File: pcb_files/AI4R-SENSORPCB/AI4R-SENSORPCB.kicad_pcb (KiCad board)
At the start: 2 copper layers, 50 x 80 mm, 25 parts, among them J10 Conn_02x10_Odd_Even, J11 USB_B_Mini, J2 Conn_01x04, J3 Conn_01x04, J4 Conn_01x04, J5 Conn_01x04, J6 Conn_02x11_Odd_Even, J7 Conn_01x03, J8 Conn_01x10, J9 Conn_01x03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

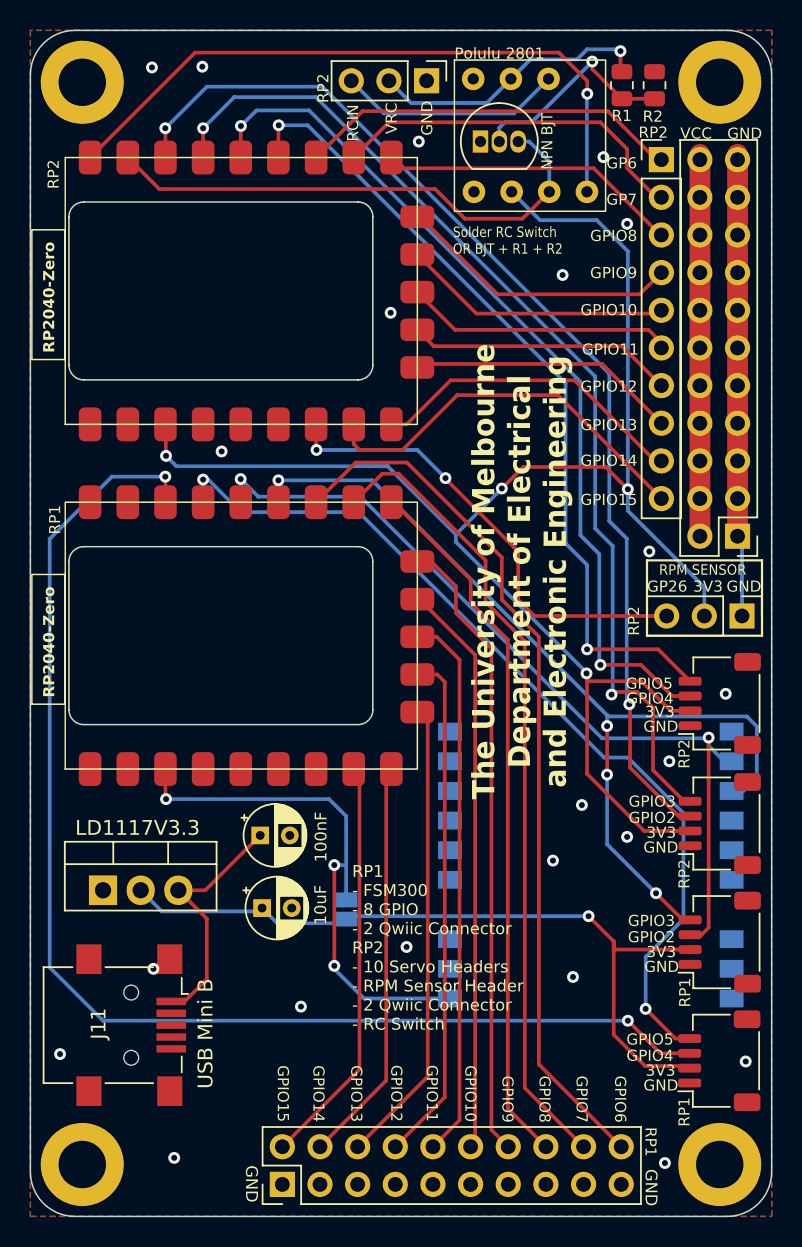
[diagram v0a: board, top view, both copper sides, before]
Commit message: fix gerber errors
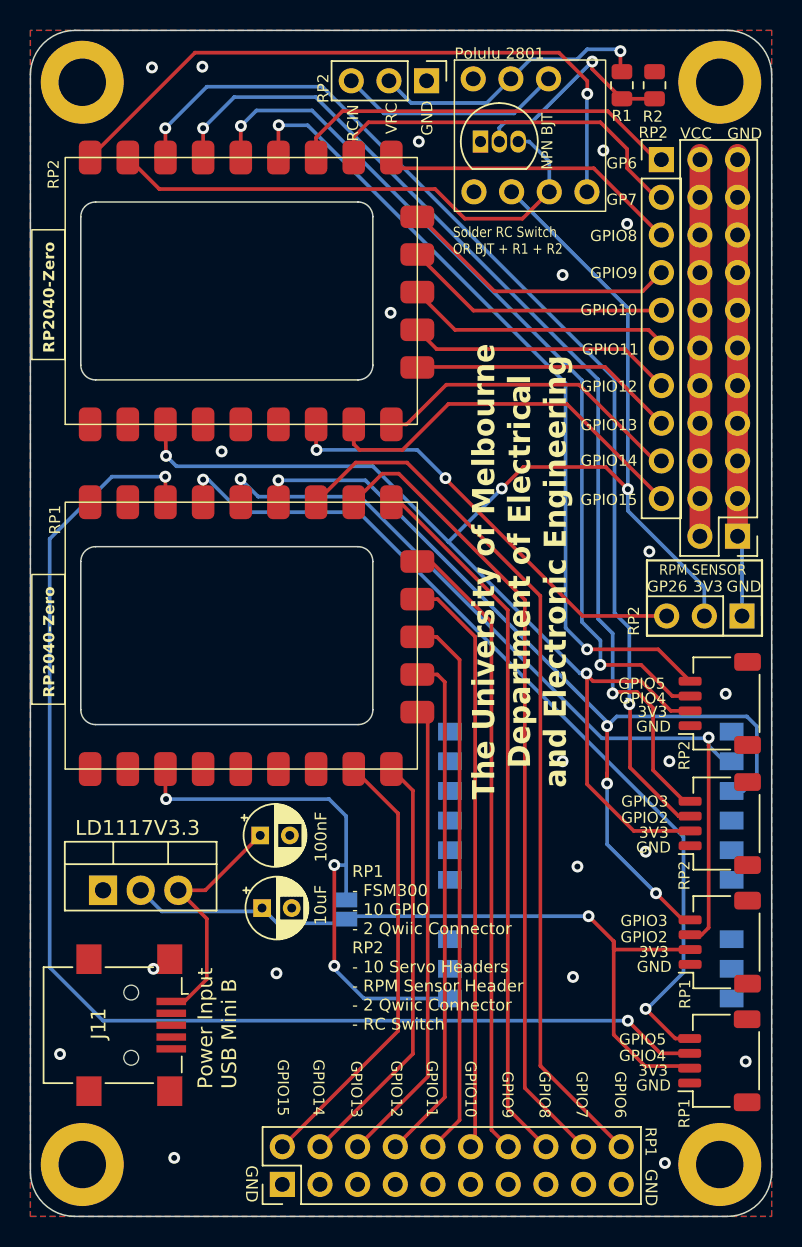
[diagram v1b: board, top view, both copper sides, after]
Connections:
- Q1 pad 3: GPIO1B -> GPIO2B
- RP2 pad 2: GPIO1B -> GPIO2B
- U2 pad 6: GPIO1B -> GPIO2B
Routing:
- net GPIO1B: track 80.3 -> 44.7 mm
- net GPIO2B: track 0.00 -> 35.6 mm
- net GP15: track 27.8 -> 29.9 mm
- net GP26B: track 31.9 -> 30.0 mm
- net 3V3B: track 111.0 -> 109.3 mm
- net GP14: track 27.5 -> 28.7 mm
- net GP10B: track 18.7 -> 17.8 mm
- net SCL2: track 61.4 -> 60.5 mm
- net GP7B: track 24.6 -> 25.4 mm
- net GP6B: track 25.9 -> 26.7 mm
- net GP10: track 38.8 -> 39.5 mm
- net SCL1: track 62.7 -> 63.2 mm
- net GND: vias 22 -> 21
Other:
- board text added: "Power Input USB Mini B"
- board text added: "RP1 - FSM300 - 10 GPIO - 2 Qwiic Connector RP2 - 10 Servo Headers - RPM Sensor Header - 2 Qwiic Connector - RC Switch"
- board text added: "Rev V1.1 Aug 2024"
- board text removed: "RP1 - FSM300 - 8 GPIO - 2 Qwiic Connector RP2 - 10 Servo Headers - RPM Sensor Header - 2 Qwiic Connector - RC Switch"
- board text removed: "Rev V1.0 June 2024"
- board text removed: "USB Mini B"
